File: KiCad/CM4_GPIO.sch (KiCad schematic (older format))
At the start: 17 parts, among them J16 GSD090012SEU, J17 Conn_02x04_Odd_Even, J18 ARJM11C7-502-AB-ER2-T, J19 Conn_02x20_Odd_Even, J20 Conn_02x04_Odd_Even, U6 74LVC1G07GW, U7 TPD4EUSB30, U8 RT9742GGJ5, U9 TPD4EUSB30

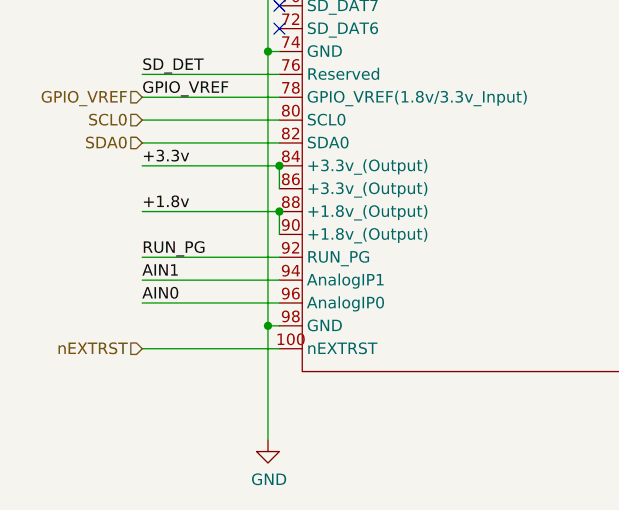
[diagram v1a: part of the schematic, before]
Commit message: PCIe Wiring, resistor value adjustments, and a bunch of small ERC fixes.
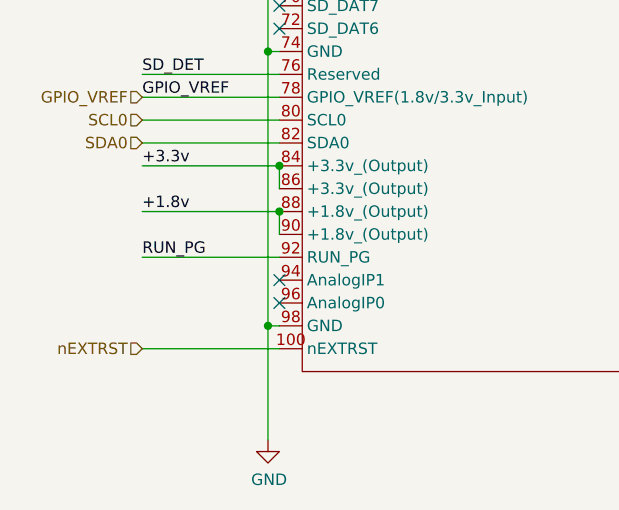
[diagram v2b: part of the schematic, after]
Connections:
- net AIN0: no longer names the net of Module1.96 (AnalogIP0)
- net AIN1: no longer names the net of Module1.94 (AnalogIP1)
- no-connect marks 8 -> 10
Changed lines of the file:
@@
 +1.8v
 Wire Wire Line
-	1600 5350 1600 5250
-Wire Wire Line
 	1600 5250 1000 5250
-Connection ~ 1600 5250
 Wire Wire Line
 	1000 5150 1600 5150
@@
 Text Label 1000 5650 0    50   ~ 0
 RUN_PG
-Text Label 1000 5750 0    50   ~ 0
-AIN1
-Text Label 1000 5850 0    50   ~ 0
-AIN0
 Text HLabel 1000 6050 0    50   Input ~ 0
 nEXTRST
@@
 Wire Wire Line
 	1550 5950 1550 4750
-Wire Wire Line
-	1600 5850 1000 5850
-Wire Wire Line
-	1000 5750 1600 5750
 Wire Wire Line
 	1600 5650 1000 5650
@@
 Wire Notes Line
 	6350 4450 6350 5250
+NoConn ~ 1600 5750
+NoConn ~ 1600 5850
+Connection ~ 1600 5250
+Wire Wire Line
+	1600 5350 1600 5250
 $EndSCHEMATC

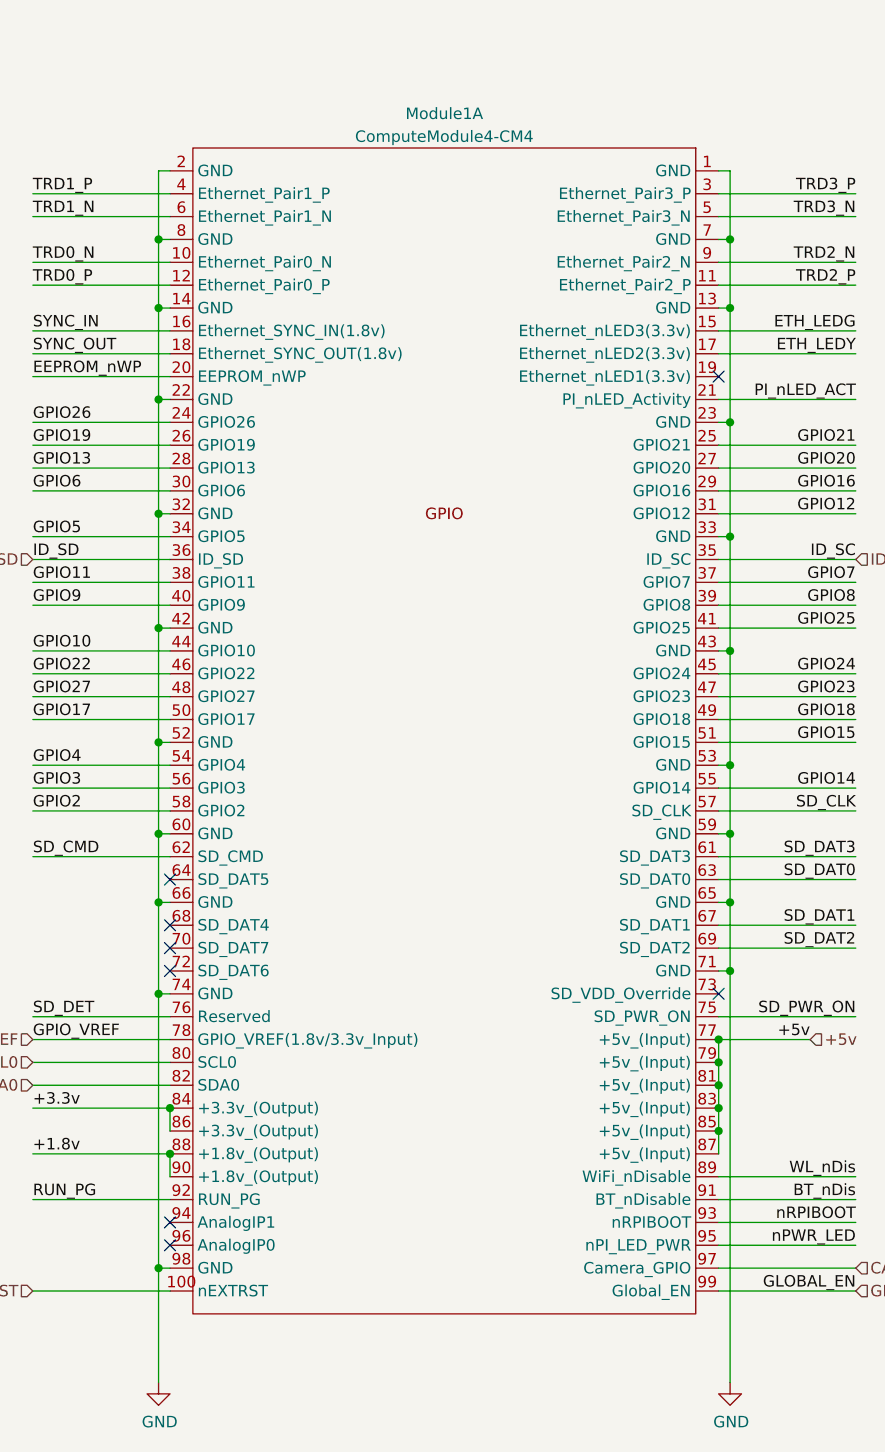
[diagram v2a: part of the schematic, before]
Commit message: Updated CM4 footprints/symbols, mounting holes
This is in a bid to make it more manufactuerable by reducing the need for explanations and questions.
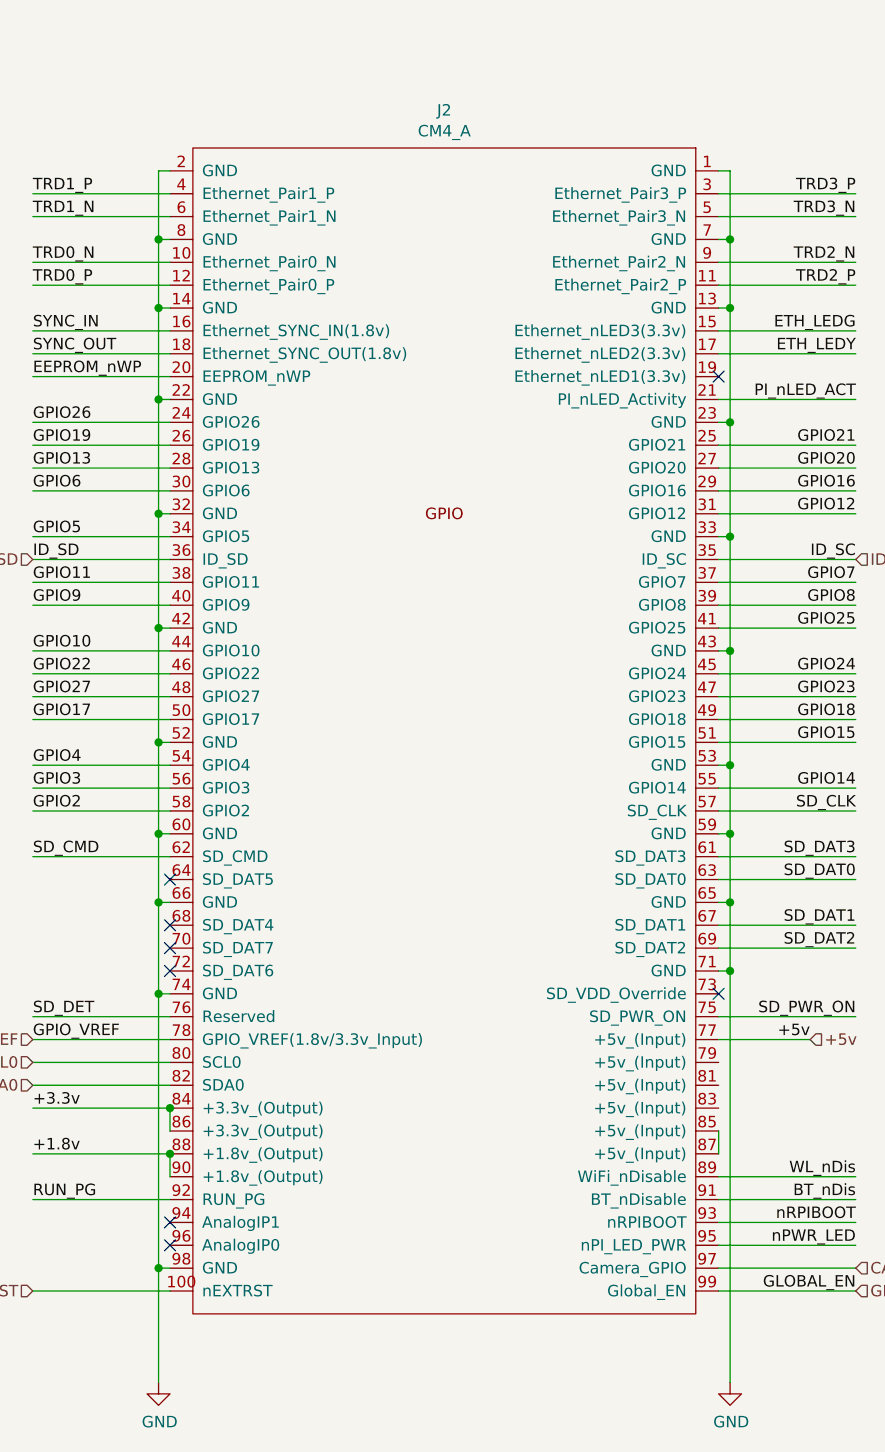
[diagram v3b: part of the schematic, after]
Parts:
- removed Module1: ComputeModule4-CM4, CM4_MATX:rpiCM4, symbol CM4_MATX:ComputeModule4-CM4
- added J2: CM4_A, CM4_MATX:DF40C100DS04V51, symbol CM4_MATX:CM4_A
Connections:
- net +1.8v: now also J2.88 (+1.8v_(Output)), J2.90 (+1.8v_(Output))
- net +3.3v: now also J2.84 (+3.3v_(Output)), J2.86 (+3.3v_(Output))
- net +5v: now also J2.77 (+5v_(Input))
- net BT_nDis: now also J2.91 (BT_nDisable)
- net CAM_GPIO: now also J2.97 (Camera_GPIO)
- net EEPROM_nWP: now also J2.20 (EEPROM_nWP)
- net ETH_LEDG: now also J2.15 (Ethernet_nLED3(3.3v))
- net ETH_LEDY: now also J2.17 (Ethernet_nLED2(3.3v))
- net GLOBAL_EN: now also J2.99 (Global_EN)
- net GND: now also J2.1 (GND), J2.13 (GND), J2.14 (GND), J2.2 (GND), J2.22 (GND), J2.23 (GND), J2.32 (GND), J2.33 (GND), J2.42 (GND), J2.43 (GND), J2.52 (GND), J2.53 (GND), J2.59 (GND), J2.60 (GND), J2.65 (GND), J2.66 (GND), J2.7 (GND), J2.71 (GND), J2.74 (GND), J2.8 (GND), J2.98 (GND)
- net GPIO10: now also J2.44 (GPIO10)
- net GPIO11: now also J2.38 (GPIO11)
- net GPIO12: now also J2.31 (GPIO12)
- net GPIO13: now also J2.28 (GPIO13)
- net GPIO14: now also J2.55 (GPIO14)
- net GPIO15: now also J2.51 (GPIO15)
- net GPIO16: now also J2.29 (GPIO16)
- net GPIO17: now also J2.50 (GPIO17)
- net GPIO18: now also J2.49 (GPIO18)
- net GPIO19: now also J2.26 (GPIO19)
- net GPIO2: now also J2.58 (GPIO2)
- net GPIO20: now also J2.27 (GPIO20)
- net GPIO21: now also J2.25 (GPIO21)
- net GPIO22: now also J2.46 (GPIO22)
- net GPIO23: now also J2.47 (GPIO23)
- net GPIO24: now also J2.45 (GPIO24)
- net GPIO25: now also J2.41 (GPIO25)
- net GPIO26: now also J2.24 (GPIO26)
- net GPIO27: now also J2.48 (GPIO27)
- net GPIO3: now also J2.56 (GPIO3)
- net GPIO4: now also J2.54 (GPIO4)
- net GPIO5: now also J2.34 (GPIO5)
- net GPIO6: now also J2.30 (GPIO6)
- net GPIO7: now also J2.37 (GPIO7)
- net GPIO8: now also J2.39 (GPIO8)
- net GPIO9: now also J2.40 (GPIO9)
- net GPIO_VREF: now also J2.78 (GPIO_VREF(1.8v/3.3v_Input))
- net ID_SC: now also J2.35 (ID_SC)
- net ID_SD: now also J2.36 (ID_SD)
- net PI_nLED_ACT: now also J2.21 (PI_nLED_Activity)
- net RUN_PG: now also J2.92 (RUN_PG)
- net SCL0: now also J2.80 (SCL0)
- net SDA0: now also J2.82 (SDA0)
- net SD_CLK: now also J2.57 (SD_CLK)
- net SD_CMD: now also J2.62 (SD_CMD)
- net SD_DAT0: now also J2.63 (SD_DAT0)
- net SD_DAT1: now also J2.67 (SD_DAT1)
- net SD_DAT2: now also J2.69 (SD_DAT2)
- net SD_DAT3: now also J2.61 (SD_DAT3)
- net SD_DET: now also J2.76 (Reserved)
- net SD_PWR_ON: now also J2.75 (SD_PWR_ON)
- net SYNC_IN: now also J2.16 (Ethernet_SYNC_IN(1.8v))
- net SYNC_OUT: now also J2.18 (Ethernet_SYNC_OUT(1.8v))
- net TRD0_N: now also J2.10 (Ethernet_Pair0_N)
- net TRD0_P: now also J2.12 (Ethernet_Pair0_P)
- net TRD1_N: now also J2.6 (Ethernet_Pair1_N)
- net TRD1_P: now also J2.4 (Ethernet_Pair1_P)
- net TRD2_N: now also J2.9 (Ethernet_Pair2_N)
- net TRD2_P: now also J2.11 (Ethernet_Pair2_P)
- net TRD3_N: now also J2.5 (Ethernet_Pair3_N)
- net TRD3_P: now also J2.3 (Ethernet_Pair3_P)
- net WL_nDis: now also J2.89 (WiFi_nDisable)
- net nEXTRST: now also J2.100 (nEXTRST)
- net nPWR_LED: now also J2.95 (nPI_LED_PWR)
- net nRPIBOOT: now also J2.93 (nRPIBOOT)
- new net: J2.85 (+5v_(Input)), J2.87 (+5v_(Input))
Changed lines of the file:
@@
 Sheet 4 16
 Title "GPIO, SDIO, PIn Headers, Ethernet"
-Date "2020-12-28"
+Date "2021-02-08"
 Rev "0.1"
 Comp "Copyright Oliver Møller/@TheGuyDanish 2020, CERN OHL-P v2"
@@
 Comment4 ""
 $EndDescr
-$Comp
-L CM4_MATX:ComputeModule4-CM4 Module1
-U 1 1 5FBC3653
-P 5650 1000
-AR Path="/5FBC3653" Ref="Module1"  Part="1"
-AR Path="/5FBC336F/5FBC3653" Ref="Module1"  Part="1"
-F 0 "Module1" H 2800 1100 50  0000 C CNN
-F 1 "ComputeModule4-CM4" H 2800 1000 50  0000 C CNN
-F 2 "CM4_MATX:rpiCM4" H 4050 850 50  0001 C CNN
-F 3 "" H 4050 850 50  0001 C CNN
-F 4 "Hirose" H 2650 1150 50  0001 C CNN "Manufacturer"
-F 5 "2x DF40C-100DS-0.4V(51)" H 2650 1050 50  0001 C CNN "Manufacturer Part Number"
-	1    5650 1000
-	1    0    0    -1
-$EndComp
 Wire Wire Line
 	4000 1150 4050 1150
@@
 $EndComp
 Wire Wire Line
-	4000 5450 4000 5350
-Connection ~ 4000 5050
-Wire Wire Line
-	4000 5050 4000 4950
-Connection ~ 4000 5150
-Wire Wire Line
-	4000 5150 4000 5050
-Connection ~ 4000 5250
-Wire Wire Line
-	4000 5250 4000 5150
-Connection ~ 4000 5350
-Wire Wire Line
-	4000 5350 4000 5250
-Wire Wire Line
 	4000 4950 4400 4950
-Connection ~ 4000 4950
 Text Label 4400 4950 2    50   ~ 0
 +5v
@@
 Wire Wire Line
 	1600 5450 1600 5550
-Connection ~ 1600 5450
 Text Label 1000 5650 0    50   ~ 0
 RUN_PG
@@
 NoConn ~ 1600 5750
 NoConn ~ 1600 5850
+Wire Wire Line
+	1600 5350 1600 5250
+$Comp
+L CM4_MATX:CM4_A J2
+U 1 1 6027D1CB
+P 1700 1050
+F 0 "J2" H 2800 1215 50  0000 C CNN
+F 1 "CM4_A" H 2800 1124 50  0000 C CNN
+F 2 "CM4_MATX:DF40C100DS04V51" H 1700 1250 50  0001 C CNN
+F 3 "https://datasheets.raspberrypi.org/cm4/cm4-datasheet.pdf" H 1700 1050 50  0001 C CNN
+	1    1700 1050
+	1    0    0    -1
+$EndComp
+Wire Wire Line
+	4000 5350 4000 5450
 Connection ~ 1600 5250
-Wire Wire Line
-	1600 5350 1600 5250
+Connection ~ 1600 5450
 $EndSCHEMATC

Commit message: Started picking passive components, overhauled library
Cleaned up a bunch of schematic library references.
Added datasheets, descriptions for a lot of existing parts.
Picked most capacitor parts, still a couple left.
Cleaned up a fair few footprint references.
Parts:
- C15: footprint (none) -> CM4_MATX:C_0603_1608Metric_Pad1.08x0.95mm_HandSolder; symbol Device:C_Small -> CM4_MATX:C_Small; Description (none) -> 6.3V 10uF X5R 0603 20% Tol; Mfr. (none) -> Samsung; Mfr. No (none) -> CL10A106MQ8NNNC; Mouser Part Number (none) -> 187-CL10A106MQ8NNNC; Mouser Price/Stock (none) -> https://www.mouser.co.uk/ProductDetail/Samsung-Electro-Mech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
- C17: footprint (none) -> CM4_MATX:C_0402_1005Metric_Pad0.74x0.62mm_HandSolder; symbol Device:C_Small -> CM4_MATX:C_Small; Description (none) -> 10V 0.1uF X5R 0402 20% Tol; Mfr. (none) -> AVX; Mfr. No (none) -> 0402ZD104MAT4A; Mouser Part Number (none) -> 581-0402ZD104MAT4A; Mouser Price/Stock (none) -> https://www.mouser.co.uk/ProductDetail/AVX/0402ZD104MAT4A/?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
- J16: Height 3.15 -> (none); Manufacturer_Name Amphenol -> (none); Manufacturer_Part_Number GSD090012SEU -> (none); Mfr. (none) -> Amphenol; Mfr. No (none) -> GSD090012SEU
- J17, J20: symbol Connector_Generic:Conn_02x04_Odd_Even -> CM4_MATX:Conn_02x04_Odd_Even; Description (none) -> Standard 2.54mm (100mil)-separated pins
- J18: Height 13.8 -> (none); Manufacturer_Name ABRACON -> (none); Manufacturer_Part_Number ARJM11C7-502-AB-ER2-T -> (none); Mfr. (none) -> ABRACON; Mfr. No (none) -> ARJM11C7-502-AB-ER2-T
- J19: symbol Connector_Generic:Conn_02x20_Odd_Even -> CM4_MATX:Conn_02x20_Odd_Even; Description (none) -> Standard 2.54mm (100mil)-separated pins
- J2: Description (none) -> Board to Board & Mezzanine Connectors 100P SMT RECEPTACLE; Mfr. (none) -> Hirose; Mfr. No (none) -> DF40C-100DS-0.4V(51); Mouser Part Number (none) -> 798-DF40C100DS0.4V51; Mouser Price/Stock (none) -> https://www.mouser.co.uk/ProductDetail/Hirose-Connector/DF4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
- JP3: Description (none) -> Standard 2.54mm (100mil)-separated pins
- R19, R20, R21, R22: symbol Device:R_Small -> CM4_MATX:R_Small
- U6: Height 1.1 -> (none); Manufacturer_Name Nexperia -> (none); Manufacturer_Part_Number 74LVC1G07GW,125 -> (none); Mfr. (none) -> Nexperia; Mfr. No (none) -> 74LVC1G07GW,125
- U7, U9: symbol Power_Protection:TPD4EUSB30 -> CM4_MATX:TPD4EUSB30; Description (none) -> ESD Suppressors / TVS Diodes 4Ch ESD SOLUTION; Mfr. (none) -> Texas Instruments; Mfr. No (none) -> TPD4EUSB30DQAR; Mouser Part Number (none) -> 595-TPD4EUSB30DQAR; Mouser Price/Stock (none) -> https://www.mouser.co.uk/ProductDetail/Texas-Instruments/TP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

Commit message: More BOM changes
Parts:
- R19: footprint (none) -> CM4_MATX:R_0402_1005Metric_Pad0.72x0.64mm_HandSolder; Description (none) -> 0402 1/16W 1KOhm 1%; Mfr. (none) -> Vishay / Dale; Mfr. No (none) -> CRCW04021K00FKEDC; Mouser Part Number (none) -> 71-CRCW04021K00FKEDC; Mouser Price/Stock (none) -> https://www.mouser.co.uk/ProductDetail/Vishay-Dale/CRCW0402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
- R20, R21: footprint (none) -> CM4_MATX:R_0402_1005Metric_Pad0.72x0.64mm_HandSolder; Description (none) -> 0402 1/16W 470Ohm 1%; Mfr. (none) -> Vishay / Dale; Mfr. No (none) -> CRCW0402470RFKEDC; Mouser Part Number (none) -> 71-CRCW0402470RFKEDC; Mouser Price/Stock (none) -> https://www.mouser.co.uk/ProductDetail/Vishay-Dale/CRCW0402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
- R22: footprint (none) -> CM4_MATX:R_0603_1608Metric_Pad0.98x0.95mm_HandSolder; Description (none) -> 0603 1/16W 12KOhm 1%; Mfr. (none) -> Vishay / Dale; Mfr. No (none) -> CRCW040212K0FKED; Mouser Part Number (none) -> 71-CRCW0402-12K-E3; Mouser Price/Stock (none) -> https://www.mouser.co.uk/ProductDetail/Vishay-Dale/CRCW0402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
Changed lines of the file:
@@
 F 0 "R20" V 10400 5050 50  0000 C CNN
 F 1 "470 1%" V 10500 5350 50  0000 C CNN
-F 2 "" H 10450 5200 50  0001 C CNN
-F 3 "~" H 10450 5200 50  0001 C CNN
+F 2 "CM4_MATX:R_0402_1005Metric_Pad0.72x0.64mm_HandSolder" H 10450 5200 50  0001 C CNN
+F 3 "https://www.mouser.co.uk/datasheet/2/427/crcwce3-1762584.pdf" H 10450 5200 50  0001 C CNN
+F 4 "0402 1/16W 470Ohm 1%" H 10450 5200 50  0001 C CNN "Description"
+F 5 "Vishay / Dale" H 10450 5200 50  0001 C CNN "Mfr."
+F 6 "CRCW0402470RFKEDC" H 10450 5200 50  0001 C CNN "Mfr. No"
+F 7 "71-CRCW0402470RFKEDC" H 10450 5200 50  0001 C CNN "Mouser Part Number"
+F 8 "https://www.mouser.co.uk/ProductDetail/Vishay-Dale/CRCW0402470RFKEDC/?qs=sGAEpiMZZMvdGkrng054t0DrEhLhGh8gS2JeFEIj4jg5iP%252BQ%2FR%2FgVQ%3D%3D" H 10450 5200 50  0001 C CNN "Mouser Price/Stock"
 	1    10450 5200
 	0    1    1    0
@@
 F 0 "R21" V 10400 5250 50  0000 C CNN
 F 1 "470 1%" V 10500 5550 50  0000 C CNN
-F 2 "" H 10450 5400 50  0001 C CNN
-F 3 "~" H 10450 5400 50  0001 C CNN
+F 2 "CM4_MATX:R_0402_1005Metric_Pad0.72x0.64mm_HandSolder" H 10450 5400 50  0001 C CNN
+F 3 "https://www.mouser.co.uk/datasheet/2/427/crcwce3-1762584.pdf" H 10450 5400 50  0001 C CNN
+F 4 "0402 1/16W 470Ohm 1%" H 10450 5400 50  0001 C CNN "Description"
+F 5 "Vishay / Dale" H 10450 5400 50  0001 C CNN "Mfr."
+F 6 "CRCW0402470RFKEDC" H 10450 5400 50  0001 C CNN "Mfr. No"
+F 7 "71-CRCW0402470RFKEDC" H 10450 5400 50  0001 C CNN "Mouser Part Number"
+F 8 "https://www.mouser.co.uk/ProductDetail/Vishay-Dale/CRCW0402470RFKEDC/?qs=sGAEpiMZZMvdGkrng054t0DrEhLhGh8gS2JeFEIj4jg5iP%252BQ%2FR%2FgVQ%3D%3D" H 10450 5400 50  0001 C CNN "Mouser Price/Stock"
 	1    10450 5400
 	0    1    1    0
@@
 F 0 "R22" H 11050 2200 50  0000 L CNN
 F 1 "12K 1%" H 10700 2300 50  0000 L CNN
-F 2 "" H 11050 2350 50  0001 C CNN
-F 3 "~" H 11050 2350 50  0001 C CNN
+F 2 "CM4_MATX:R_0603_1608Metric_Pad0.98x0.95mm_HandSolder" H 11050 2350 50  0001 C CNN
+F 3 "https://www.mouser.co.uk/datasheet/2/427/dcrcwe3-1762152.pdf" H 11050 2350 50  0001 C CNN
+F 4 "0603 1/16W 12KOhm 1%" H 11050 2350 50  0001 C CNN "Description"
+F 5 "Vishay / Dale" H 11050 2350 50  0001 C CNN "Mfr."
+F 6 "CRCW040212K0FKED" H 11050 2350 50  0001 C CNN "Mfr. No"
+F 7 "71-CRCW0402-12K-E3" H 11050 2350 50  0001 C CNN "Mouser Part Number"
+F 8 "https://www.mouser.co.uk/ProductDetail/Vishay-Dale/CRCW040212K0FKED/?qs=sGAEpiMZZMvdGkrng054txEw7b1YnvGuGxPcVgtIGNs%3D" H 11050 2350 50  0001 C CNN "Mouser Price/Stock"
 	1    11050 2350
 	1    0    0    -1
@@
 F 0 "R19" H 6900 3350 50  0000 C CNN
 F 1 "1K 1%" H 6650 3200 50  0000 C CNN
-F 2 "" H 6800 3250 50  0001 C CNN
-F 3 "~" H 6800 3250 50  0001 C CNN
+F 2 "CM4_MATX:R_0402_1005Metric_Pad0.72x0.64mm_HandSolder" H 6800 3250 50  0001 C CNN
+F 3 "https://www.mouser.co.uk/datasheet/2/427/crcwce3-1762584.pdf" H 6800 3250 50  0001 C CNN
+F 4 "0402 1/16W 1KOhm 1%" H 6800 3250 50  0001 C CNN "Description"
+F 5 "Vishay / Dale" H 6800 3250 50  0001 C CNN "Mfr."
+F 6 "CRCW04021K00FKEDC" H 6800 3250 50  0001 C CNN "Mfr. No"
+F 7 "71-CRCW04021K00FKEDC" H 6800 3250 50  0001 C CNN "Mouser Part Number"
+F 8 "https://www.mouser.co.uk/ProductDetail/Vishay-Dale/CRCW04021K00FKEDC/?qs=sGAEpiMZZMvdGkrng054t0DrEhLhGh8gZ6wm0HkRlDUT6OA9YCnj9w%3D%3D" H 6800 3250 50  0001 C CNN "Mouser Price/Stock"
 	1    6800 3250
 	1    0    0    -1
